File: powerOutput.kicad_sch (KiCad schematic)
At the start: 16 parts, among them J1 Screw_Terminal_01x02, J10 Screw_Terminal_01x04, J11 Screw_Terminal_01x04, J12 Screw_Terminal_01x04, J13 Conn_01x16_Pin, J9 Screw_Terminal_01x04, K1 SANYOU_SRD-S-124DM, K2 SANYOU_SRD-S-124DM, K3 SANYOU_SRD-S-124DM, K4 SANYOU_SRD-S-124DM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

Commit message: merged seperate projects
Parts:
- removed J13: Conn_01x16_Pin, symbol Connector:Conn_01x16_Pin
- removed K1, K2, K3, K4, K5, K6, K7, K8: SANYOU_SRD-S-124DM, Relay_THT:Relay_SPST_SANYOU_SRD_Series_Form_A, symbol Relay:SANYOU_SRD_Form_A
- added K1, K2, K3, K4, K5, K6, K7, K8: SANYOU_SRD-S-124D, Relay_THT:Relay_SPDT_SANYOU_SRD_Series_Form_C, symbol Relay:SANYOU_SRD_Form_C
- added TP1, TP11, TP14, TP2, TP3, TP4, TP5, TP6, TP7, TP8: ~, symbol Connector:TestPoint
- added TP10: DO12, symbol Connector:TestPoint
- added TP9: DO11, symbol Connector:TestPoint
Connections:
- net at J11.1 (Pin_1): now also K5.3
- net at J11.2 (Pin_2): now also K5.1
- net at J11.3 (Pin_3): now also K6.3
- net at J11.4 (Pin_4): now also K6.1
- net at J12.4 (Pin_4): now also K8.1
- net at J12.3 (Pin_3): now also K8.3
- net at U4.11 (O8): now also K8.5, TP8.1
- net at J9.1 (Pin_1): now also K1.3
- net at J9.2 (Pin_2): now also K1.1
- net at J9.3 (Pin_3): now also K2.3
- net at J9.4 (Pin_4): now also K2.1
- net at J1.1 (Pin_1), U7.18 (O1): now also TP11.1
- net at J1.2 (Pin_2), U7.17 (O2): now also TP14.1
- net at U4.18 (O1): now also K1.5, TP1.1
- net at J10.4 (Pin_4): now also K4.1
- net at J10.3 (Pin_3): now also K4.3
- net at U4.15 (O4): now also K4.5, TP4.1
- net DO9: now reaches U7.1 (I1)
- net at U7.15 (O4): now also TP10.1
- net at U7.16 (O3): now also TP9.1
- net DO10: now reaches U7.2 (I2)
- net DO11: now reaches U7.3 (I3)
- net DO12: now reaches U7.4 (I4)
- net at U4.17 (O2): now also K2.5, TP2.1
- net at U4.14 (O5): now also K5.5
- net DO1: now reaches U4.1 (I1)
- net DO2: now reaches U4.2 (I2)
- net DO3: now reaches U4.3 (I3)
- net DO4: now reaches U4.4 (I4)
- net DO5: now reaches U4.5 (I5)
- net DO6: now reaches U4.6 (I6)
- net DO7: now reaches U4.7 (I7)
- net DO8: now reaches U4.8 (I8)
- net at J10.2 (Pin_2): now also K3.1
- net at J10.1 (Pin_1): now also K3.3
- net at U4.16 (O3): now also K3.5, TP3.1
- net at U4.13 (O6): now also K6.5, TP5.1, TP6.1
- net at J12.2 (Pin_2): now also K7.1
- net at J12.1 (Pin_1): now also K7.3
- net at U4.12 (O7): now also K7.5, TP7.1
- net +24V renamed COM
- net COM: now also K1.2, K2.2, K3.2, K4.2, K5.2, K6.2, K7.2, K8.2
- no-connect marks 0 -> 16

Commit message: added part numbers
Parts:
- J1: footprint (none) -> Connector_Phoenix_MC:PhoenixContact_MC_1,5_2-G-3.5_1x02_P3.50mm_Horizontal; LCSC (none) -> C61791
- J10, J11, J12, J9: footprint (none) -> Connector_Phoenix_MC:PhoenixContact_MC_1,5_4-G-3.5_1x04_P3.50mm_Horizontal; LCSC (none) -> C5241865
- K1, K2, K3, K4, K5, K6, K7, K8: LCSC (none) -> C276436
- U4, U7: footprint (none) -> Package_SO:SOIC-20W_7.5x12.8mm_P1.27mm; LCSC (none) -> C7494313
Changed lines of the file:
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@@
 			)
 		)
-		(property "Footprint" ""
+		(property "Footprint" "Connector_Phoenix_MC:PhoenixContact_MC_1,5_4-G-3.5_1x04_P3.50mm_Horizontal"
 			(at 168.91 104.14 0)
 			(effects
@@
 		)
 		(property "Description" "Generic screw terminal, single row, 01x04, script generated (kicad-library-utils/schlib/autogen/connector/)"
+			(at 168.91 104.14 0)
+			(effects
+				(font
+					(size 1.27 1.27)
+				)
+				(hide yes)
+			)
+		)
+		(property "LCSC" "C5241865"
 			(at 168.91 104.14 0)
 			(effects
@@
 			)
 		)
+		(property "LCSC" "C276436"
+			(at 129.54 21.59 0)
+			(effects
+				(font
+					(size 1.27 1.27)
+				)
+				(hide yes)
+			)
+		)
 		(pin "4"
 		)
@@
 			)
 		)
+		(property "LCSC" "C276436"
+			(at 129.54 151.13 0)
+			(effects
+				(font
+					(size 1.27 1.27)
+				)
+				(hide yes)
+			)
+		)
 		(pin "4"
 		)
@@
 			)
 		)
-		(property "Footprint" ""
+		(property "Footprint" "Connector_Phoenix_MC:PhoenixContact_MC_1,5_4-G-3.5_1x04_P3.50mm_Horizontal"
 			(at 168.91 30.48 0)
 			(effects
@@
 			)
 		)
+		(property "LCSC" "C5241865"
+			(at 168.91 30.48 0)
+			(effects
+				(font
+					(size 1.27 1.27)
+				)
+				(hide yes)
+			)
+		)
 		(pin "4"
 		)
@@
 			)
 		)
-		(property "Footprint" ""
+		(property "Footprint" "Connector_Phoenix_MC:PhoenixContact_MC_1,5_2-G-3.5_1x02_P3.50mm_Horizontal"
 			(at 101.6 172.72 0)
 			(effects
@@
 		)
 		(property "Description" "Generic screw terminal, single row, 01x02, script generated (kicad-library-utils/schlib/autogen/connector/)"
+			(at 101.6 172.72 0)
+			(effects
+				(font
+					(size 1.27 1.27)
+				)
+				(hide yes)
+			)
+		)
+		(property "LCSC" "C61791"
 			(at 101.6 172.72 0)
 			(effects
@@
 			)
 		)
+		(property "LCSC" "C276436"
+			(at 129.54 77.47 0)
+			(effects
+				(font
+					(size 1.27 1.27)
+				)
+				(hide yes)
+			)
+		)
 		(pin "4"
 		)
@@
 			)
 		)
+		(property "LCSC" "C276436"
+			(at 129.54 95.25 0)
+			(effects
+				(font
+					(size 1.27 1.27)
+				)
+				(hide yes)
+			)
+		)
 		(pin "4"
 		)
@@
 			)
 		)
-		(property "Footprint" ""
+		(property "Footprint" "Package_SO:SOIC-20W_7.5x12.8mm_P1.27mm"
 			(at 57.15 157.48 0)
 			(effects
@@
 		)
 		(property "Description" "Darlington Transistor Arrays, SOIC18/DIP18"
+			(at 55.88 140.97 0)
+			(effects
+				(font
+					(size 1.27 1.27)
+				)
+				(hide yes)
+			)
+		)
+		(property "LCSC" "C7494313"
 			(at 55.88 140.97 0)
 			(effects
@@
 			)
 		)
+		(property "LCSC" "C276436"
+			(at 129.54 132.08 0)
+			(effects
+				(font
+					(size 1.27 1.27)
+				)
+				(hide yes)
+			)
+		)
 		(pin "4"
 		)
@@
 			)
 		)
+		(property "LCSC" "C276436"
+			(at 129.54 40.64 0)
+			(effects
+				(font
+					(size 1.27 1.27)
+				)
+				(hide yes)
+			)
+		)
 		(pin "4"
 		)
@@
 			)
 		)
+		(property "LCSC" "C276436"
+			(at 129.54 114.3 0)
+			(effects
+				(font
+					(size 1.27 1.27)
+				)
+				(hide yes)
+			)
+		)
 		(pin "4"
 		)
@@
 			)
 		)
-		(property "Footprint" ""
+		(property "Footprint" "Connector_Phoenix_MC:PhoenixContact_MC_1,5_4-G-3.5_1x04_P3.50mm_Horizontal"
 			(at 168.91 67.31 0)
 			(effects
@@
 		)
 		(property "Description" "Generic screw terminal, single row, 01x04, script generated (kicad-library-utils/schlib/autogen/connector/)"
+			(at 168.91 67.31 0)
+			(effects
+				(font
+					(size 1.27 1.27)
+				)
+				(hide yes)
+			)
+		)
+		(property "LCSC" "C5241865"
 			(at 168.91 67.31 0)
 			(effects
@@
 			)
 		)
-		(property "Footprint" ""
+		(property "Footprint" "Connector_Phoenix_MC:PhoenixContact_MC_1,5_4-G-3.5_1x04_P3.50mm_Horizontal"
 			(at 168.91 140.97 0)
 			(effects
@@
 		)
 		(property "Description" "Generic screw terminal, single row, 01x04, script generated (kicad-library-utils/schlib/autogen/connector/)"
+			(at 168.91 140.97 0)
+			(effects
+				(font
+					(size 1.27 1.27)
+				)
+				(hide yes)
+			)
+		)
+		(property "LCSC" "C5241865"
 			(at 168.91 140.97 0)
 			(effects
@@
 			)
 		)
-		(property "Footprint" ""
+		(property "Footprint" "Package_SO:SOIC-20W_7.5x12.8mm_P1.27mm"
 			(at 57.15 99.06 0)
 			(effects
@@
 		)
 		(property "Description" "Darlington Transistor Arrays, SOIC18/DIP18"
+			(at 55.88 82.55 0)
+			(effects
+				(font
+					(size 1.27 1.27)
+				)
+				(hide yes)
+			)
+		)
+		(property "LCSC" "C7494313"
 			(at 55.88 82.55 0)
 			(effects
@@
 			(at 129.54 58.42 0)
 			(effects
+				(font
+					(size 1.27 1.27)
+				)
+				(hide yes)
+			)
+		)
+		(property "LCSC" "C276436"
+			(at 129.54 58.42 0)
+			(effects

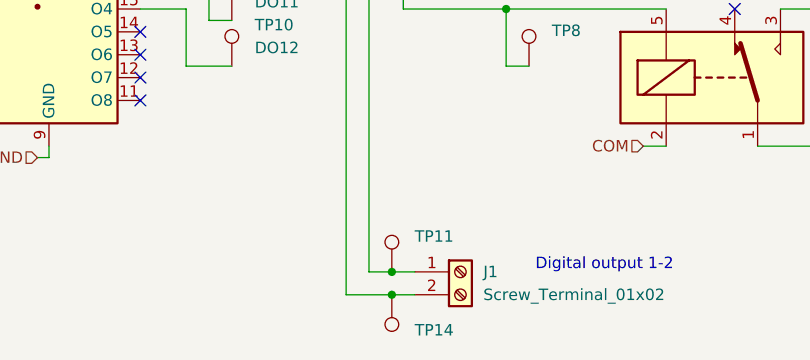
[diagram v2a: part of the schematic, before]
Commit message: larger pcb
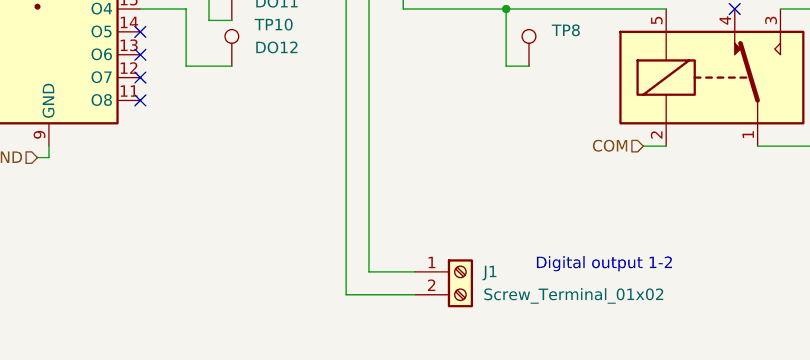
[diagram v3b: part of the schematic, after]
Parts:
- removed TP11, TP14: ~, symbol Connector:TestPoint
- TP1, TP2, TP3, TP4, TP5, TP6, TP7, TP8: footprint (none) -> TestPoint:TestPoint_Pad_D1.5mm
- TP10, TP9: footprint (none) -> TestPoint:TestPoint_Plated_Hole_D2.0mm
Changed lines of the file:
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@@
 	)
 	(junction
-		(at 93.98 175.26)
-		(diameter 0)
-		(color 0 0 0 0)
-	)
-	(junction
 		(at 106.68 77.47)
 		(diameter 0)
@@
 	)
 	(junction
-		(at 93.98 172.72)
-		(diameter 0)
-		(color 0 0 0 0)
-	)
-	(junction
 		(at 106.68 13.97)
 		(diameter 0)
@@
 	(wire
 		(pts
-			(xy 93.98 175.26) (xy 96.52 175.26)
+			(xy 88.9 175.26) (xy 96.52 175.26)
 		)
 		(stroke
@@
 	(wire
 		(pts
-			(xy 93.98 172.72) (xy 96.52 172.72)
+			(xy 91.44 172.72) (xy 96.52 172.72)
 		)
 		(stroke
@@
 	(wire
 		(pts
-			(xy 88.9 175.26) (xy 93.98 175.26)
-		)
-		(stroke
-			(width 0)
-			(type default)
-		)
-	)
-	(wire
-		(pts
 			(xy 109.22 149.86) (xy 106.68 149.86)
 		)
@@
 	(wire
 		(pts
-			(xy 91.44 172.72) (xy 93.98 172.72)
-		)
-		(stroke
-			(width 0)
-			(type default)
-		)
-	)
-	(wire
-		(pts
 			(xy 163.83 121.92) (xy 134.62 121.92)
 		)
@@
 			)
 		)
-		(property "Footprint" ""
+		(property "Footprint" "TestPoint:TestPoint_Plated_Hole_D2.0mm"
 			(at 81.28 144.78 0)
 			(effects
@@
 			)
 		)
+		(property "LCSC" ""
+			(at 76.2 144.78 0)
+			(effects
+				(font
+					(size 1.27 1.27)
+				)
+				(hide yes)
+			)
+		)
 		(pin "1"
 		)
@@
 			)
 		)
-		(property "Footprint" ""
+		(property "Footprint" "TestPoint:TestPoint_Pad_D1.5mm"
 			(at 114.3 149.86 0)
 			(effects
@@
 			)
 		)
+		(property "LCSC" ""
+			(at 109.22 149.86 0)
+			(effects
+				(font
+					(size 1.27 1.27)
+				)
+				(hide yes)
+			)
+		)
 		(pin "1"
 		)
@@
 			)
 		)
-		(property "Footprint" ""
+		(property "Footprint" "TestPoint:TestPoint_Pad_D1.5mm"
 			(at 114.3 130.81 0)
 			(effects
@@
 			)
 		)
+		(property "LCSC" ""
+			(at 109.22 130.81 0)
+			(effects
+				(font
+					(size 1.27 1.27)
+				)
+				(hide yes)
+			)
+		)
 		(pin "1"
 		)
@@
 			)
 		)
-		(property "Footprint" ""
+		(property "Footprint" "TestPoint:TestPoint_Pad_D1.5mm"
 			(at 114.3 113.03 0)
 			(effects
@@
 			)
 		)
+		(property "LCSC" ""
+			(at 109.22 113.03 0)
+			(effects
+				(font
+					(size 1.27 1.27)
+				)
+				(hide yes)
+			)
+		)
 		(pin "1"
 		)
@@
 			)
 		)
-		(property "Footprint" ""
+		(property "Footprint" "TestPoint:TestPoint_Pad_D1.5mm"
 			(at 114.3 40.64 0)
 			(effects
@@
 			)
 		)
+		(property "LCSC" ""
+			(at 109.22 40.64 0)
+			(effects
+				(font
+					(size 1.27 1.27)
+				)
+				(hide yes)
+			)
+		)
 		(pin "1"
 		)
@@
 			)
 		)
-		(property "Footprint" ""
+		(property "Footprint" "TestPoint:TestPoint_Plated_Hole_D2.0mm"
 			(at 81.28 149.86 0)
 			(effects
@@
 			)
 		)
-		(pin "1"
-		)
-		(instances
-			(project "controesp"
-				(path "/aa25b9ad-b1cb-4070-bd5f-fd163558ccd7/525bd36e-8e0f-45f3-ae1f-4768f65c2e68"
-					(reference "TP10")
-					(unit 1)
-				)
-			)
-		)
-	)
-	(symbol
-		(lib_id "Connector:TestPoint")
-		(at 93.98 172.72 0)
-		(unit 1)
-		(exclude_from_sim no)
-		(in_bom yes)
-		(on_board yes)
-		(dnp no)
-		(property "Reference" "TP11"
-			(at 96.52 168.7829 0)
-			(effects
-				(font
-					(size 1.27 1.27)
-				)
-				(justify left)
-			)
-		)
-		(property "Value" "~"
-			(at 91.44 76.962 0)
-			(effects
-				(font
-					(size 1.27 1.27)
-				)
-				(justify left)
-			)
-		)
-		(property "Footprint" ""
-			(at 99.06 172.72 0)
-			(effects
-				(font
-					(size 1.27 1.27)
-				)
-				(hide yes)
-			)
-		)
-		(property "Datasheet" "~"
-			(at 99.06 172.72 0)
-			(effects
-				(font
-					(size 1.27 1.27)
-				)
-				(hide yes)
-			)
-		)
-		(property "Description" "test point"
-			(at 93.98 172.72 0)
+		(property "LCSC" ""
+			(at 76.2 149.86 0)
 			(effects
 				(font
@@
 			(project "controesp"
 				(path "/aa25b9ad-b1cb-4070-bd5f-fd163558ccd7/525bd36e-8e0f-45f3-ae1f-4768f65c2e68"
-					(reference "TP11")
+					(reference "TP10")
 					(unit 1)
 				)
@@
 			)
 		)
-		(property "Footprint" ""
+		(property "Footprint" "TestPoint:TestPoint_Pad_D1.5mm"
 			(at 114.3 20.32 0)
 			(effects
@@
 			)
 		)
+		(property "LCSC" ""
+			(at 109.22 20.32 0)
+			(effects
+				(font
+					(size 1.27 1.27)
+				)
+				(hide yes)
+			)
+		)
 		(pin "1"
 		)
@@
 			)
 		)
-		(property "Footprint" ""
+		(property "Footprint" "TestPoint:TestPoint_Pad_D1.5mm"
 			(at 114.3 77.47 0)
 			(effects
@@
 			)
 		)
+		(property "LCSC" ""
+			(at 109.22 77.47 0)
+			(effects
+				(font
+					(size 1.27 1.27)
+				)
+				(hide yes)
+			)
+		)
 		(pin "1"
 		)
@@
 			)
 		)
-		(property "Footprint" ""
+		(property "Footprint" "TestPoint:TestPoint_Pad_D1.5mm"
 			(at 114.3 93.98 0)
 			(effects
@@
 			)
 		)
-		(pin "1"
-		)
-		(instances
-			(project "controesp"
-				(path "/aa25b9ad-b1cb-4070-bd5f-fd163558ccd7/525bd36e-8e0f-45f3-ae1f-4768f65c2e68"
-					(reference "TP5")
-					(unit 1)
-				)
-			)
-		)
-	)
-	(symbol
-		(lib_id "Connector:TestPoint")
-		(at 93.98 175.26 0)
-		(mirror x)
-		(unit 1)
-		(exclude_from_sim no)
-		(in_bom yes)
-		(on_board yes)
-		(dnp no)
-		(property "Reference" "TP14"
-			(at 96.52 179.1971 0)
-			(effects
-				(font
-					(size 1.27 1.27)
-				)
-				(justify left)
-			)
-		)
-		(property "Value" "~"
-			(at 91.44 271.018 0)
-			(effects
-				(font
-					(size 1.27 1.27)
-				)
-				(justify left)
-			)
-		)
-		(property "Footprint" ""
-			(at 99.06 175.26 0)
-			(effects
-				(font
-					(size 1.27 1.27)
-				)
-				(hide yes)
-			)
-		)
-		(property "Datasheet" "~"
-			(at 99.06 175.26 0)
-			(effects
-				(font
-					(size 1.27 1.27)
-				)
-				(hide yes)
-			)
-		)
-		(property "Description" "test point"
-			(at 93.98 175.26 0)
+		(property "LCSC" ""
+			(at 109.22 93.98 0)
 			(effects
 				(font
@@
 			(project "controesp"
 				(path "/aa25b9ad-b1cb-4070-bd5f-fd163558ccd7/525bd36e-8e0f-45f3-ae1f-4768f65c2e68"
-					(reference "TP14")
+					(reference "TP5")
 					(unit 1)
 				)
@@
 			)
 		)
-		(property "Footprint" ""
+		(property "Footprint" "TestPoint:TestPoint_Pad_D1.5mm"
 			(at 114.3 57.15 0)
 			(effects
@@
 			(at 109.22 57.15 0)
 			(effects
+				(font
+					(size 1.27 1.27)
+				)
+				(hide yes)
+			)
+		)
+		(property "LCSC" ""
+			(at 109.22 57.15 0)
+			(effects
